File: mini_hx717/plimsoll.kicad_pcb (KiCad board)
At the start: 4 copper layers, 16.3 x 29.1 mm, 17 parts, among them J1 Conn_02x06_Odd_Even, J3 Loadd Cell, U5 RS3236-3.3, U6 HX717

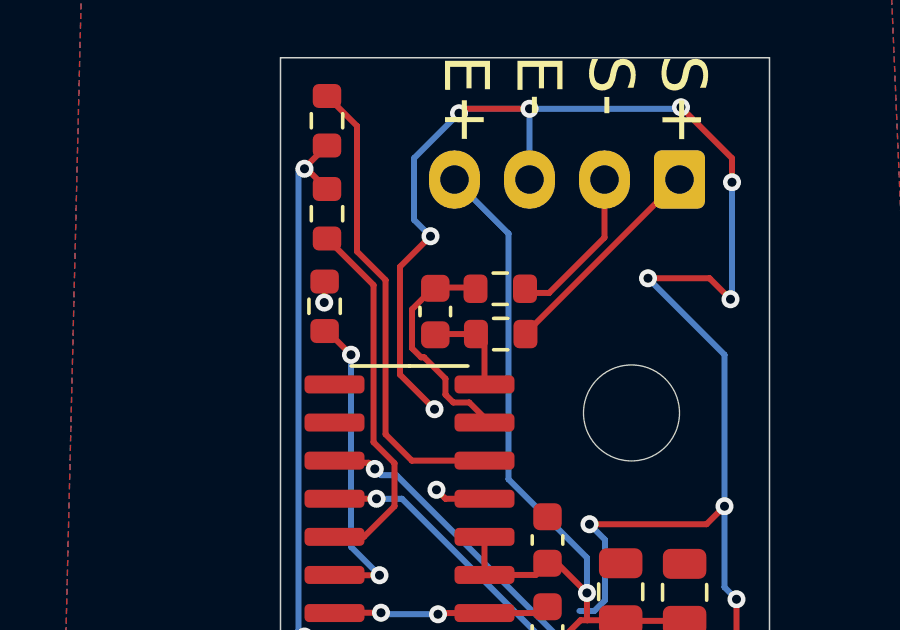
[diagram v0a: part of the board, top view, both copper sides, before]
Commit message: ads1220 added
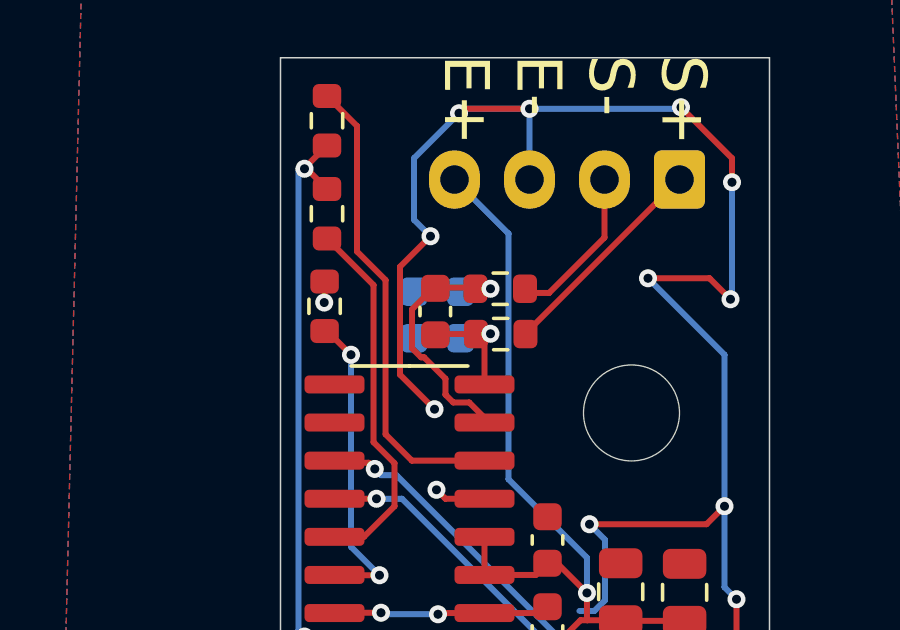
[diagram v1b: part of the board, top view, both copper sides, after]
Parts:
- added C1: DNP, Capacitor_SMD:C_0603_1608Metric, B.Cu at (30.1, 27.8)
- added C2: DNP, Capacitor_SMD:C_0603_1608Metric, B.Cu at (30.1, 29.4)
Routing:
- net Net-(U6-INA+): track 3.16 -> 4.71 mm, vias 0 -> 1
- net Net-(U6-INA-): track 7.58 -> 9.12 mm, vias 0 -> 1

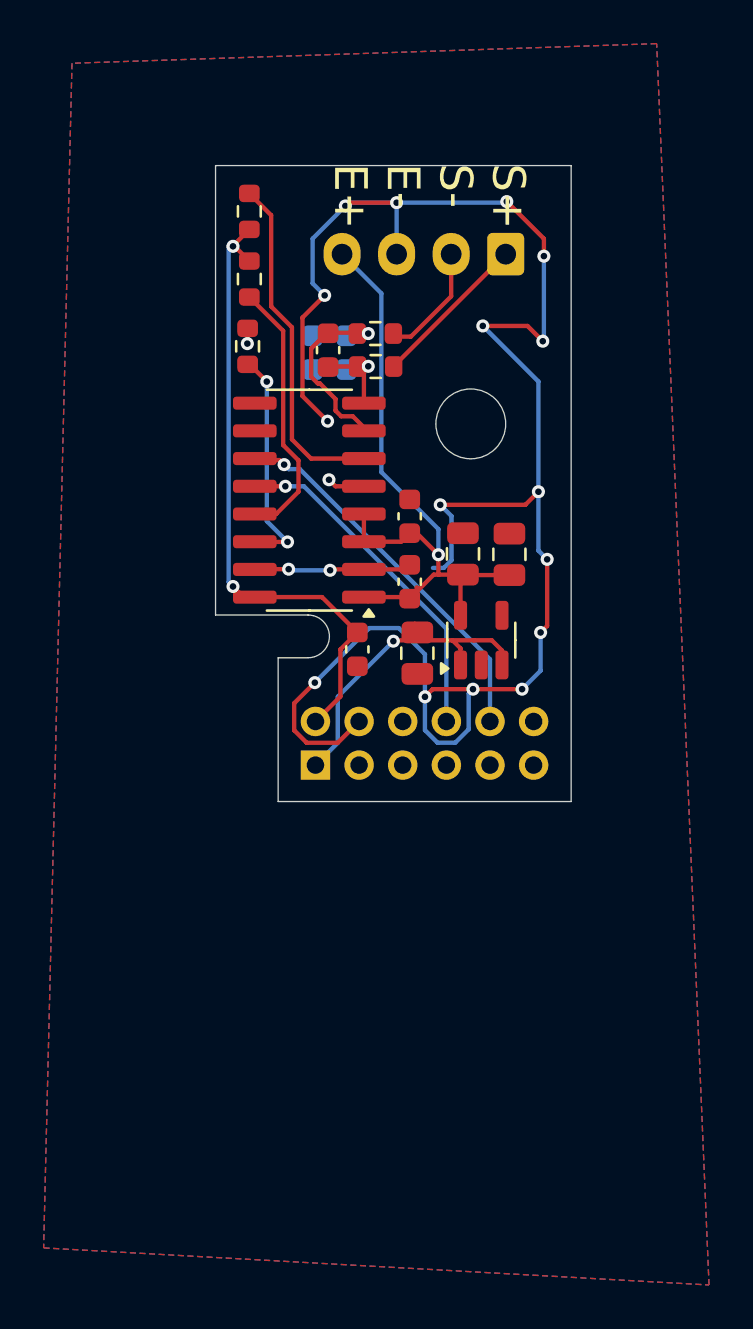
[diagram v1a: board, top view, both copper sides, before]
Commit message: Rewire connector pins and update silkscreen labels
Reassigned connector pin nets to match new signal mapping, updated silkscreen text to reflect the new pin order, and adjusted related PCB traces and vias. Also made minor component placement tweaks and cleaned up net routing for improved clarity and accuracy.
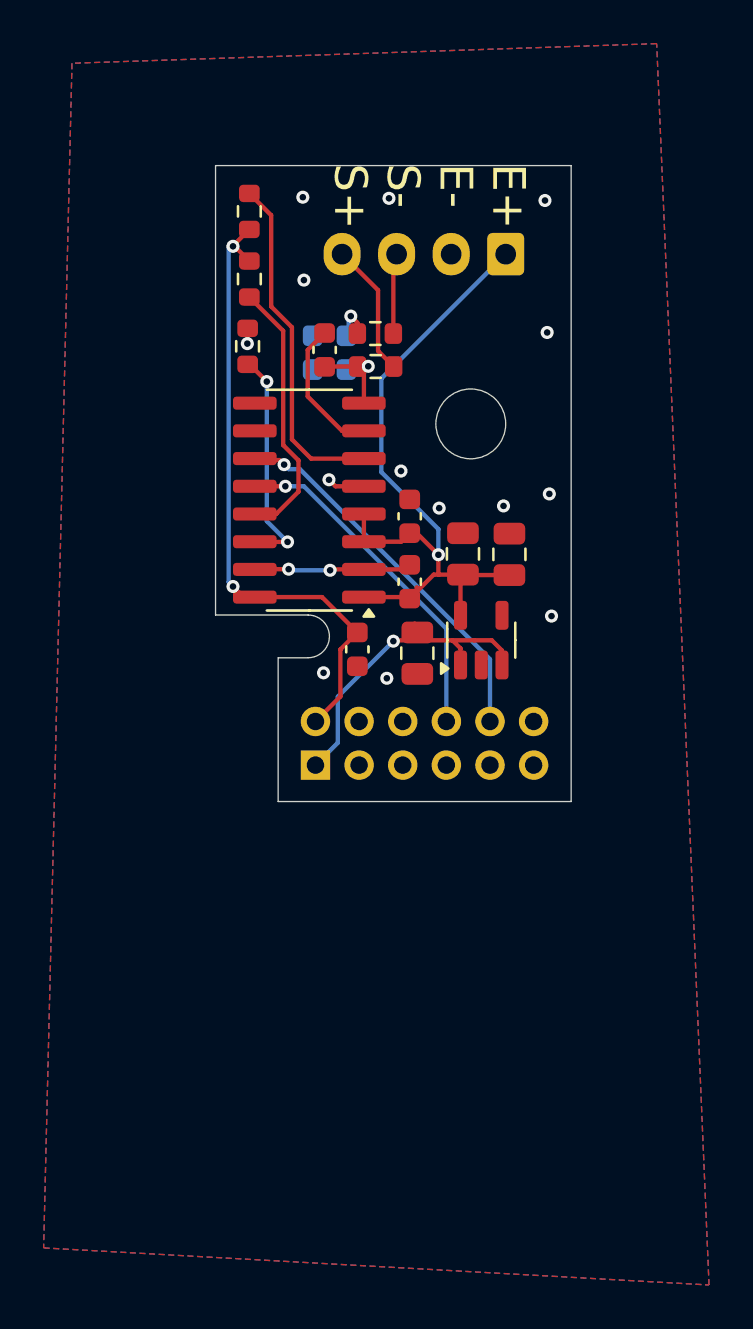
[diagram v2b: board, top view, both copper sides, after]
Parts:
- moved C7 0.16 mm to (29.9, 28.4)
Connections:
- J3 pad 1: /Signal+ -> +3.3VADC
- J3 pad 2: /Signal- -> GND
- J3 pad 3: GND -> /Signal-
- J3 pad 4: +3.3VADC -> /Signal+
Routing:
- net GND: track 95.9 -> 9.67 mm, vias 20 -> 16
- net /Signal-: track 5.41 -> 3.70 mm
- net +3.3VADC: track 31.2 -> 32.8 mm
- net /Signal+: track 7.28 -> 6.13 mm
- net Net-(U6-INA-): track 9.12 -> 8.37 mm
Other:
- board text added: "E+ E- S- S+"
- board text removed: "S+ S- E- E+"
